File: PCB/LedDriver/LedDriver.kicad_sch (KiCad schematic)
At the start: 28 parts, among them J101 LCD, J102 TweLite-R, J103 Conn_01x02_Male, J104 Conn_01x08_Male, J105 Conn_01x08_Male, J106 Conn_01x08_Male, J107 Conn_01x02_Male, J108 Barrel_Jack_Switch, J109 Conn_01x02_Male, J110 Conn_01x02_Male, SW101 SW_Push, SW102 SW_Push, SW103 SW_Push, SW104 SW_Push, SW105 SW_Push, SW106 SW_Push, SW107 SW_Push, U101 MW-R-WX

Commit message: 基板改良
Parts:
- removed C104: 0.1u, Capacitor_SMD:C_0603_1608Metric, symbol Device:C
- removed C105: 47u, Capacitor_SMD:C_0603_1608Metric, symbol Device:C
- removed J102: TweLite-R, Connector_PinSocket_2.54mm:PinSocket_1x06_P2.54mm_Vertical, symbol Connector:Conn_01x06_Male
- added C102: 10u, Capacitor_SMD:C_0603_1608Metric, symbol Device:C_Small
- added C103: 0.1u, Capacitor_SMD:C_0603_1608Metric, symbol Device:C
- added C106, C107, C108: 10u, Capacitor_SMD:C_0603_1608Metric, symbol Device:C
- added H105: MountingHole, MountingHole:MountingHole_6.4mm_M6, symbol Mechanical:MountingHole
- added J102: Conn_01x07_Female, Connector_PinSocket_2.54mm:PinSocket_1x07_P2.54mm_Vertical, symbol Connector:Conn_01x07_Female
- added J111: Conn_01x02_Male, Connector_JST:JST_XH_B2B-XH-A_1x02_P2.50mm_Vertical, symbol Connector:Conn_01x02_Male
- added U102: LM1117-3.3, Package_TO_SOT_SMD:SOT-223-3_TabPin2, symbol Regulator_Linear:LM1117-3.3
- J107: renamed from J108; value Barrel_Jack_Switch -> DC+5V
- renumbered C102 to C104, C103 to C105, J107 to J104, J109 to J105, J110 to J106, J104 to J108, J105 to J109, J106 to J110
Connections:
- net +3.3V: now also C102.2, C103.1, C107.1, U102.2 (VO); no longer J107.1
- net GND: now also C102.1, C103.2, C106.2, C107.2, C108.2, J102.1 (Pin_1), J111.2 (Pin_2), U102.1 (GND)
- net PRG: now also J102.3 (Pin_3)
- net RESET: now also J102.5 (Pin_5)
- net RX: now also J102.4 (Pin_4)
- net TX: now also J102.2 (Pin_2)
- net at J103.1 (Pin_1): now also J102.6 (Pin_6)
- new net: C106.1, C108.1, J107.1, J111.1 (Pin_1), U102.3 (VI)
- no-connect marks 10 -> 11
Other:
- moved on the sheet: C101, C104, C105, H101, H102, H103, H104, J101, J103, J104, J105, J106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

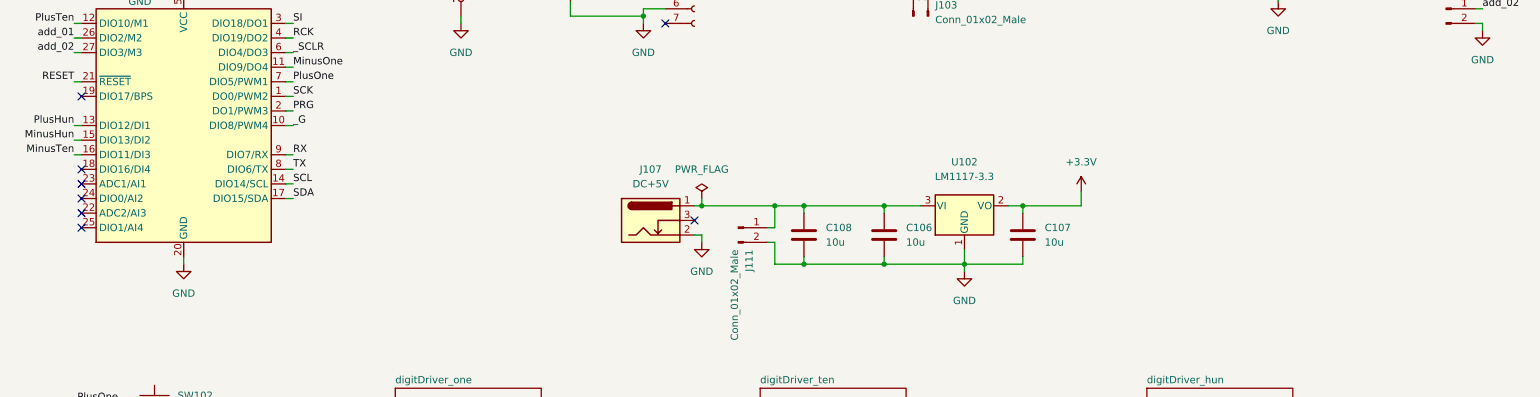
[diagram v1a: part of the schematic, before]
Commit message: 回路修正
三端子レギュレータ追加
GNDパターン修正
currentパターン同士のクリアランスを確保
ファン端子追加
温度センサ追加
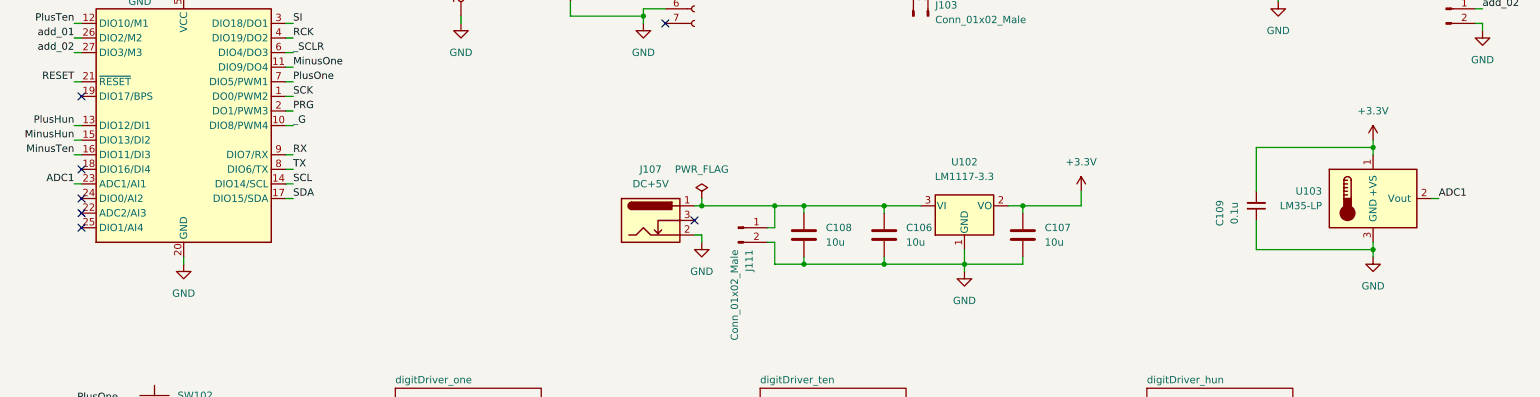
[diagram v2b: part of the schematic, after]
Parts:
- added C109: 0.1u, Capacitor_SMD:C_0603_1608Metric, symbol Device:C_Small
- added U103: LM35-LP, symbol Sensor_Temperature:LM35-LP
- SW101, SW102, SW103, SW104, SW105, SW106, SW107: footprint Button_Switch_SMD:SW_SPST_B3S-1000 -> Library:SW_SPST_B3S-1000
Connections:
- net +3.3V: now also C109.2, U103.1 (+VS)
- net GND: now also C109.1, U103.3 (GND)
- net ADC1: now reaches U101.23 (ADC1/AI1)
- net ADC1: now also U103.2 (Vout)
- no-connect marks 11 -> 10

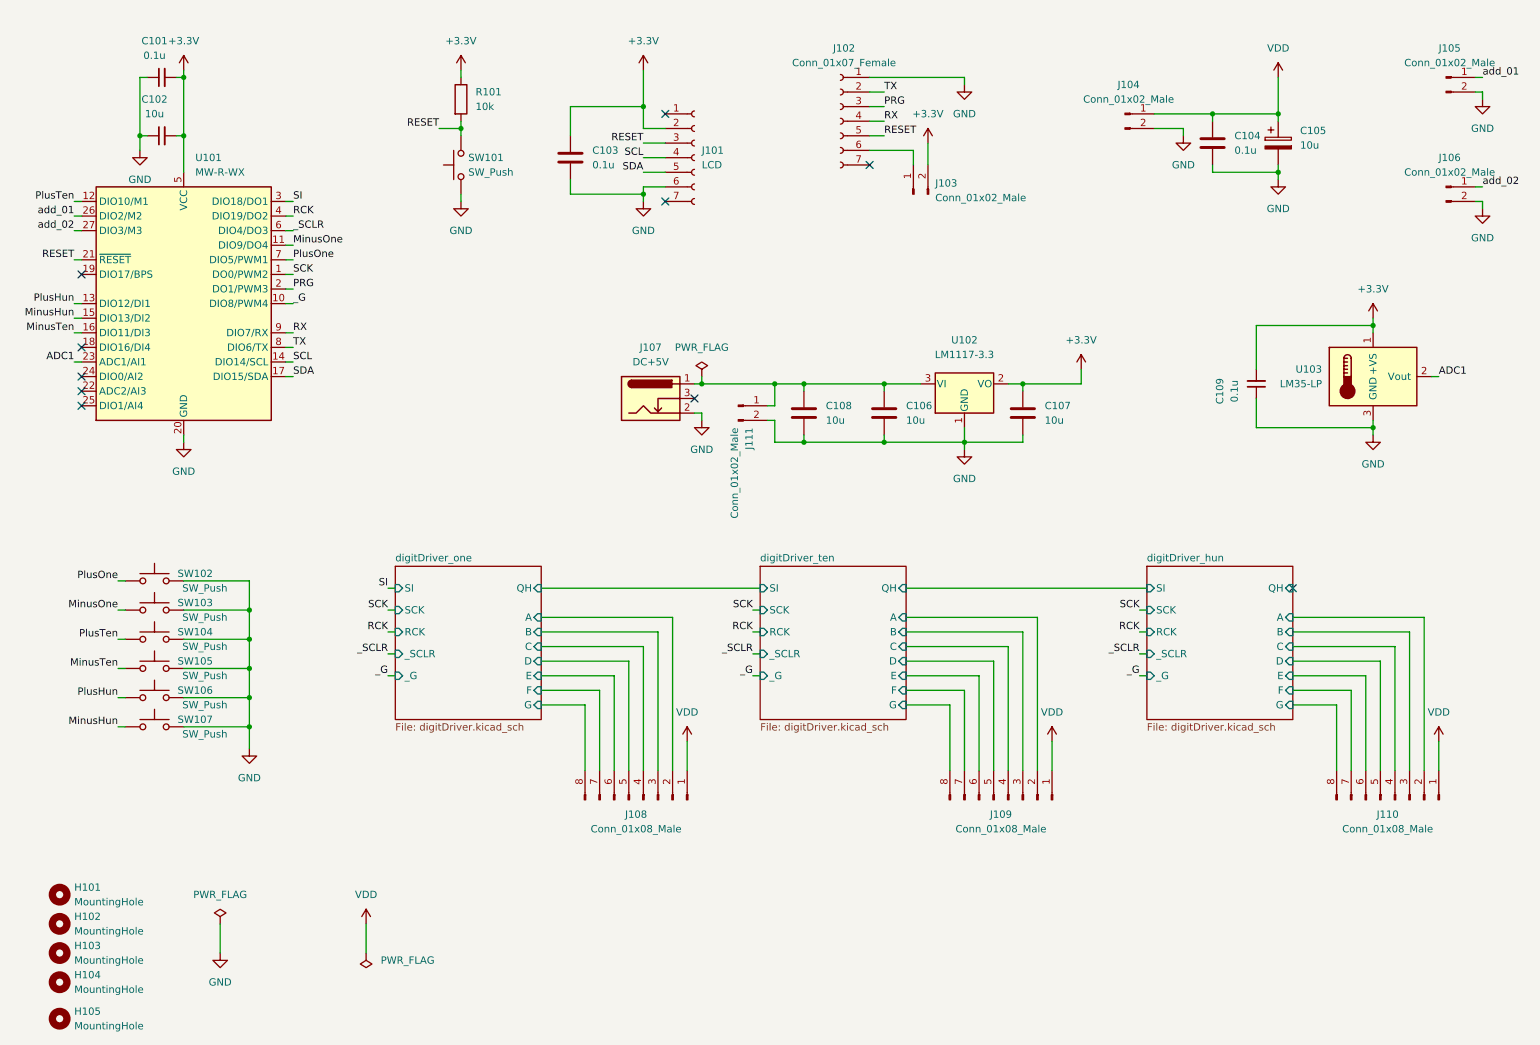
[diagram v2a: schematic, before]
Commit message: パターン修正
LEDドライバのパスコンを最短で配線
LEDドライバのタブをGNDに配線
平行な信号パターン同士の距離を開け、GNDパターンを間に追加
直角なパターンを修正
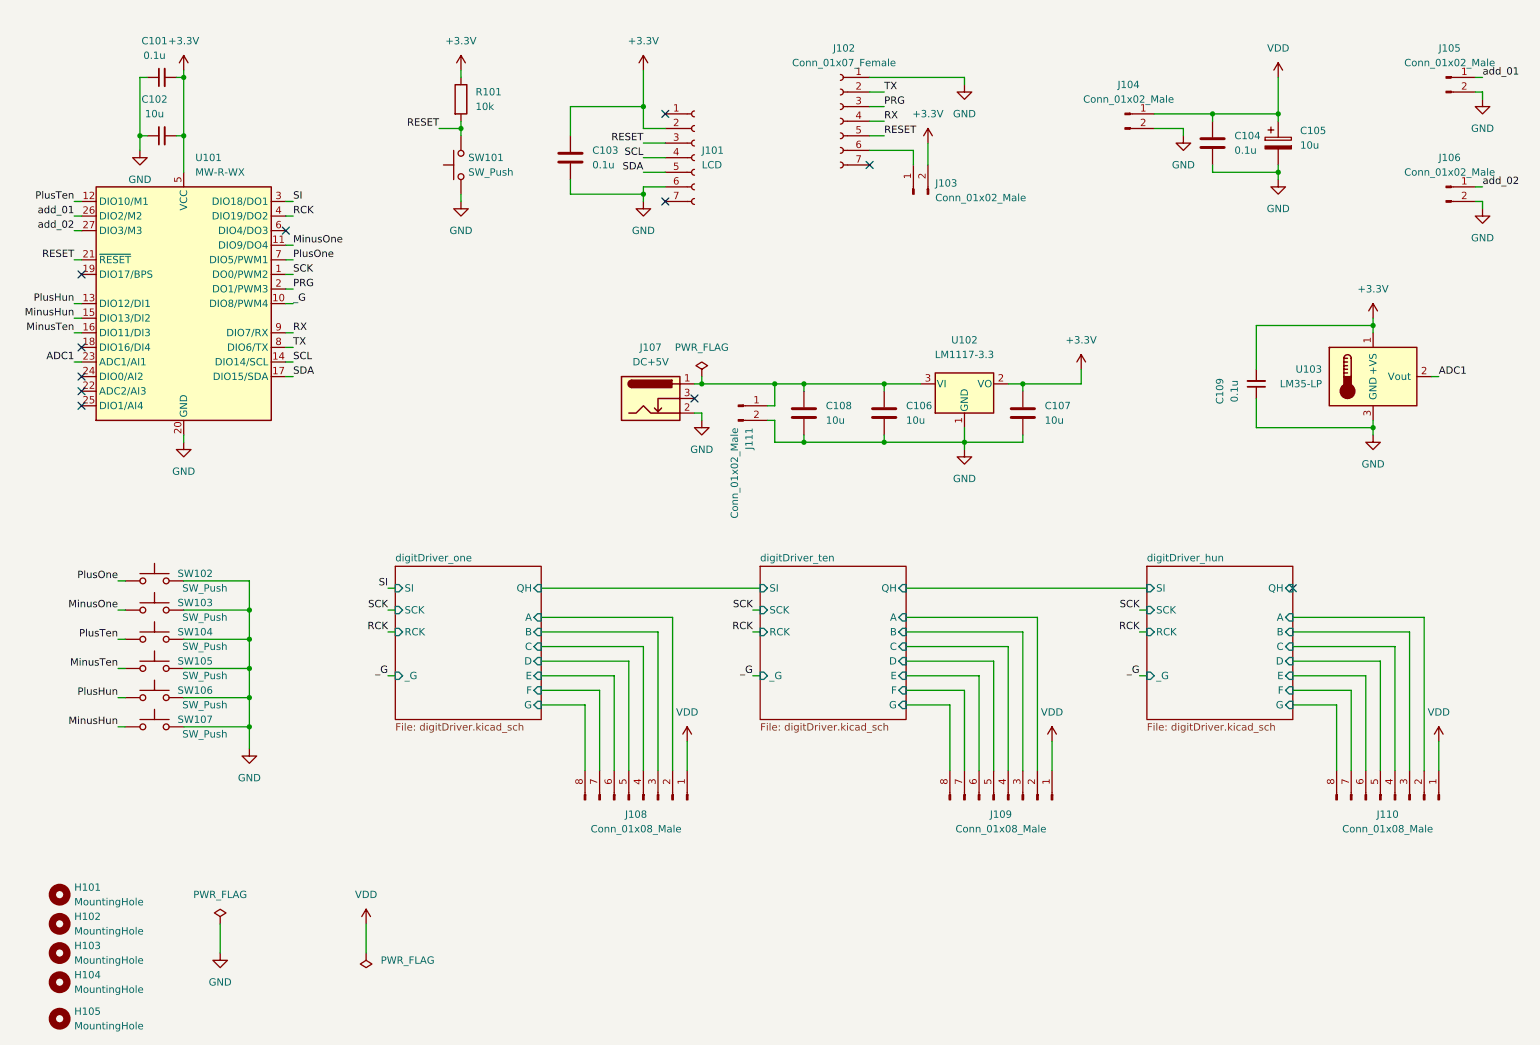
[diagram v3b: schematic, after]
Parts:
- U103: footprint (none) -> Package_TO_SOT_THT:TO-92_Inline_Horizontal1
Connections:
- net _SCLR: no longer names the net of U101.6 (DIO4/DO3)
- no-connect marks 10 -> 11
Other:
- sheet digitDriver_hun ports: added none; removed _SCLR
- sheet digitDriver_one ports: added none; removed _SCLR
- sheet digitDriver_ten ports: added none; removed _SCLR
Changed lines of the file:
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@@
   (no_connect (at 29.21 83.82))
   (no_connect (at 29.21 81.28))
+  (no_connect (at 64.77 55.88))
   (no_connect (at 130.81 50.8))
   (no_connect (at 135.89 85.09))
@@
     (stroke (width 0) (type default) (color 0 0 0 0))
   )
-  (wire (pts (xy 64.77 55.88) (xy 66.04 55.88))
-    (stroke (width 0) (type default) (color 0 0 0 0))
-  )
   (wire (pts (xy 254 72.39) (xy 254 73.66))
     (stroke (width 0) (type default) (color 0 0 0 0))
@@
     (stroke (width 0) (type default) (color 0 0 0 0))
   )
-  (wire (pts (xy 82.55 129.54) (xy 83.82 129.54))
-    (stroke (width 0) (type default) (color 0 0 0 0))
-  )
   (wire (pts (xy 182.88 92.71) (xy 182.88 93.98))
     (stroke (width 0) (type default) (color 0 0 0 0))
@@
     (stroke (width 0) (type default) (color 0 0 0 0))
   )
-  (wire (pts (xy 146.05 129.54) (xy 147.32 129.54))
-    (stroke (width 0) (type default) (color 0 0 0 0))
-  )
   (wire (pts (xy 166.37 36.83) (xy 168.91 36.83))
     (stroke (width 0) (type default) (color 0 0 0 0))
@@
   )
   (wire (pts (xy 190.5 82.55) (xy 193.04 82.55))
-    (stroke (width 0) (type default) (color 0 0 0 0))
-  )
-  (wire (pts (xy 213.36 129.54) (xy 214.63 129.54))
     (stroke (width 0) (type default) (color 0 0 0 0))
   )
@@
     (effects (font (size 1.27 1.27)) (justify right bottom))
   )
-  (label "_SCLR" (at 146.05 129.54 180)
-    (effects (font (size 1.27 1.27)) (justify right bottom))
-  )
   (label "SI" (at 66.04 50.8 0)
     (effects (font (size 1.27 1.27)) (justify left bottom))
   )
-  (label "_SCLR" (at 213.36 129.54 180)
-    (effects (font (size 1.27 1.27)) (justify right bottom))
-  )
   (label "RCK" (at 146.05 125.73 180)
     (effects (font (size 1.27 1.27)) (justify right bottom))
@@
     (effects (font (size 1.27 1.27)) (justify right bottom))
   )
-  (label "_SCLR" (at 66.04 55.88 0)
-    (effects (font (size 1.27 1.27)) (justify left bottom))
-  )
   (label "SCK" (at 146.05 121.92 180)
-    (effects (font (size 1.27 1.27)) (justify right bottom))
-  )
-  (label "_SCLR" (at 82.55 129.54 180)
     (effects (font (size 1.27 1.27)) (justify right bottom))
   )
@@
       (effects (font (size 1.27 1.27)) (justify right))
     )
-    (property "Footprint" "" (id 2) (at 255.27 87.63 0)
+    (property "Footprint" "Package_TO_SOT_THT:TO-92_Inline_Horizontal1" (id 2) (at 255.27 87.63 0)
       (effects (font (size 1.27 1.27)) (justify left) hide)
     )
@@
       (effects (font (size 1.27 1.27)) (justify left))
     )
-    (pin "_SCLR" input (at 214.63 129.54 180)
-      (effects (font (size 1.27 1.27)) (justify left))
-    )
     (pin "SI" input (at 214.63 118.11 180)
       (effects (font (size 1.27 1.27)) (justify left))
@@
       (effects (font (size 1.27 1.27)) (justify left))
     )
-    (pin "_SCLR" input (at 147.32 129.54 180)
-      (effects (font (size 1.27 1.27)) (justify left))
-    )
     (pin "SI" input (at 147.32 118.11 180)
       (effects (font (size 1.27 1.27)) (justify left))
@@
       (effects (font (size 1.27 1.27)) (justify left))
     )
-    (pin "_SCLR" input (at 83.82 129.54 180)
-      (effects (font (size 1.27 1.27)) (justify left))
-    )
     (pin "SI" input (at 83.82 118.11 180)
       (effects (font (size 1.27 1.27)) (justify left))
@@
       (reference "#PWR0439") (unit 1) (value "GND") (footprint "")
     )
+    (path "/67d089be-80a1-4b77-b39f-7287a2db11d8/d8818bbe-48f0-473f-9c8f-9df4557a2604"
+      (reference "#PWR?") (unit 1) (value "+3.3V") (footprint "")
+    )
+    (path "/e8372379-4f81-4714-a4bd-0da8f876e2d2/d8818bbe-48f0-473f-9c8f-9df4557a2604"
+      (reference "#PWR?") (unit 1) (value "+3.3V") (footprint "")
+    )
+    (path "/6a3af4d5-d6c8-45cb-bbe0-393f0deb387e/d8818bbe-48f0-473f-9c8f-9df4557a2604"
+      (reference "#PWR?") (unit 1) (value "+3.3V") (footprint "")
+    )
     (path "/f611c082-111a-4b50-92ff-deff296724dc"

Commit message: 穴位置移動
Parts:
- H101, H102, H103, H104: footprint MountingHole:MountingHole_3mm -> MountingHole:MountingHole_3.2mm_M3
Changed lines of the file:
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@@
       (effects (font (size 1.27 1.27)) (justify left))
     )
-    (property "Footprint" "MountingHole:MountingHole_3mm" (id 2) (at 25.4 171.45 0)
+    (property "Footprint" "MountingHole:MountingHole_3.2mm_M3" (id 2) (at 25.4 171.45 0)
       (effects (font (size 1.27 1.27)) hide)
     )
@@
       (effects (font (size 1.27 1.27)) (justify left))
     )
-    (property "Footprint" "MountingHole:MountingHole_3mm" (id 2) (at 25.4 186.69 0)
+    (property "Footprint" "MountingHole:MountingHole_3.2mm_M3" (id 2) (at 25.4 186.69 0)
       (effects (font (size 1.27 1.27)) hide)
     )
@@
       (effects (font (size 1.27 1.27)) (justify left))
     )
-    (property "Footprint" "MountingHole:MountingHole_3mm" (id 2) (at 25.4 176.53 0)
+    (property "Footprint" "MountingHole:MountingHole_3.2mm_M3" (id 2) (at 25.4 176.53 0)
       (effects (font (size 1.27 1.27)) hide)
     )
@@
       (effects (font (size 1.27 1.27)) (justify left))
     )
-    (property "Footprint" "MountingHole:MountingHole_3mm" (id 2) (at 25.4 181.61 0)
+    (property "Footprint" "MountingHole:MountingHole_3.2mm_M3" (id 2) (at 25.4 181.61 0)
       (effects (font (size 1.27 1.27)) hide)
     )
@@
       (reference "#PWR0125") (unit 1) (value "GND") (footprint "")
     )
+    (path "/e8372379-4f81-4714-a4bd-0da8f876e2d2/d8818bbe-48f0-473f-9c8f-9df4557a2604"
+      (reference "#PWR0126") (unit 1) (value "+3.3V") (footprint "")
+    )
+    (path "/6a3af4d5-d6c8-45cb-bbe0-393f0deb387e/d8818bbe-48f0-473f-9c8f-9df4557a2604"
+      (reference "#PWR0127") (unit 1) (value "+3.3V") (footprint "")
+    )
+    (path "/67d089be-80a1-4b77-b39f-7287a2db11d8/d8818bbe-48f0-473f-9c8f-9df4557a2604"
+      (reference "#PWR0128") (unit 1) (value "+3.3V") (footprint "")
+    )
     (path "/e8372379-4f81-4714-a4bd-0da8f876e2d2/7fbde03d-bca5-4c17-9b34-3f56ffbb2c6f"
       (reference "#PWR0201") (unit 1) (value "GND") (footprint "")
@@
       (reference "#PWR0439") (unit 1) (value "GND") (footprint "")
     )
-    (path "/67d089be-80a1-4b77-b39f-7287a2db11d8/d8818bbe-48f0-473f-9c8f-9df4557a2604"
-      (reference "#PWR?") (unit 1) (value "+3.3V") (footprint "")
-    )
-    (path "/e8372379-4f81-4714-a4bd-0da8f876e2d2/d8818bbe-48f0-473f-9c8f-9df4557a2604"
-      (reference "#PWR?") (unit 1) (value "+3.3V") (footprint "")
-    )
-    (path "/6a3af4d5-d6c8-45cb-bbe0-393f0deb387e/d8818bbe-48f0-473f-9c8f-9df4557a2604"
-      (reference "#PWR?") (unit 1) (value "+3.3V") (footprint "")
-    )
     (path "/f611c082-111a-4b50-92ff-deff296724dc"
       (reference "C101") (unit 1) (value "0.1u") (footprint "Capacitor_SMD:C_0603_1608Metric")
@@
     )
     (path "/5c86494f-8b0f-4cd5-9d71-9e827be728e0"
-      (reference "H101") (unit 1) (value "MountingHole") (footprint "MountingHole:MountingHole_3mm")
+      (reference "H101") (unit 1) (value "MountingHole") (footprint "MountingHole:MountingHole_3.2mm_M3")
     )
     (path "/a6450fc2-0c7e-49c4-a909-a7cadc910e3a"
-      (reference "H102") (unit 1) (value "MountingHole") (footprint "MountingHole:MountingHole_3mm")
+      (reference "H102") (unit 1) (value "MountingHole") (footprint "MountingHole:MountingHole_3.2mm_M3")
     )
     (path "/eeb57c59-27bd-4b66-983e-819791e6d7df"
-      (reference "H103") (unit 1) (value "MountingHole") (footprint "MountingHole:MountingHole_3mm")
+      (reference "H103") (unit 1) (value "MountingHole") (footprint "MountingHole:MountingHole_3.2mm_M3")
     )
     (path "/7e976bb6-b36f-478a-8a8b-ee2127a8a13e"
-      (reference "H104") (unit 1) (value "MountingHole") (footprint "MountingHole:MountingHole_3mm")
+      (reference "H104") (unit 1) (value "MountingHole") (footprint "MountingHole:MountingHole_3.2mm_M3")
     )
     (path "/76c6fb69-0fe3-42b3-afbd-47a4ef169770"
